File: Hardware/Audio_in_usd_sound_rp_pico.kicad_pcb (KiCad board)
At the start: 2 copper layers, 100 x 100 mm, 275 parts, among them J1 ADC IN, J11 SDR ANT, J12 SDR Out, J13 ANT_BNC, J14 ANT_BNC, J15 Audio IN, J16 Audio IN, J17 Mini-jack socket, J4 Conn_02x20_Counter_Clockwise, J5 Conn_01x20, J6 Conn_01x20, J7 Conn_02x20_Counter_Clockwise, J8 BNC, Q1 MMBT2222A 1P, Q2 MMBT2222A 1P, Q3 MMBT2222A, SW1 Left, SW2 Right, T1 Screw Terminal, 4Px5.08mm, 20A, T2 Screw Terminal, 4Px5.08mm, 20A, U1 LSM6DSO32TR, U10 Si4732, U11 HS96L03W2C03, U12 L298N, U13 LM393DR2G, U15 DS18B20A10T6, U17 LM2937xS, U2 PCM1808PWR, U3 Pico, U4 MS5351M, U5 CJ431, U6 TSOP4438, U7 PI5C3253CQEX, U8 OPA1612AxD, U9 LM358, X1 Q13FC1350000400, Y1 X322525MSB4SI

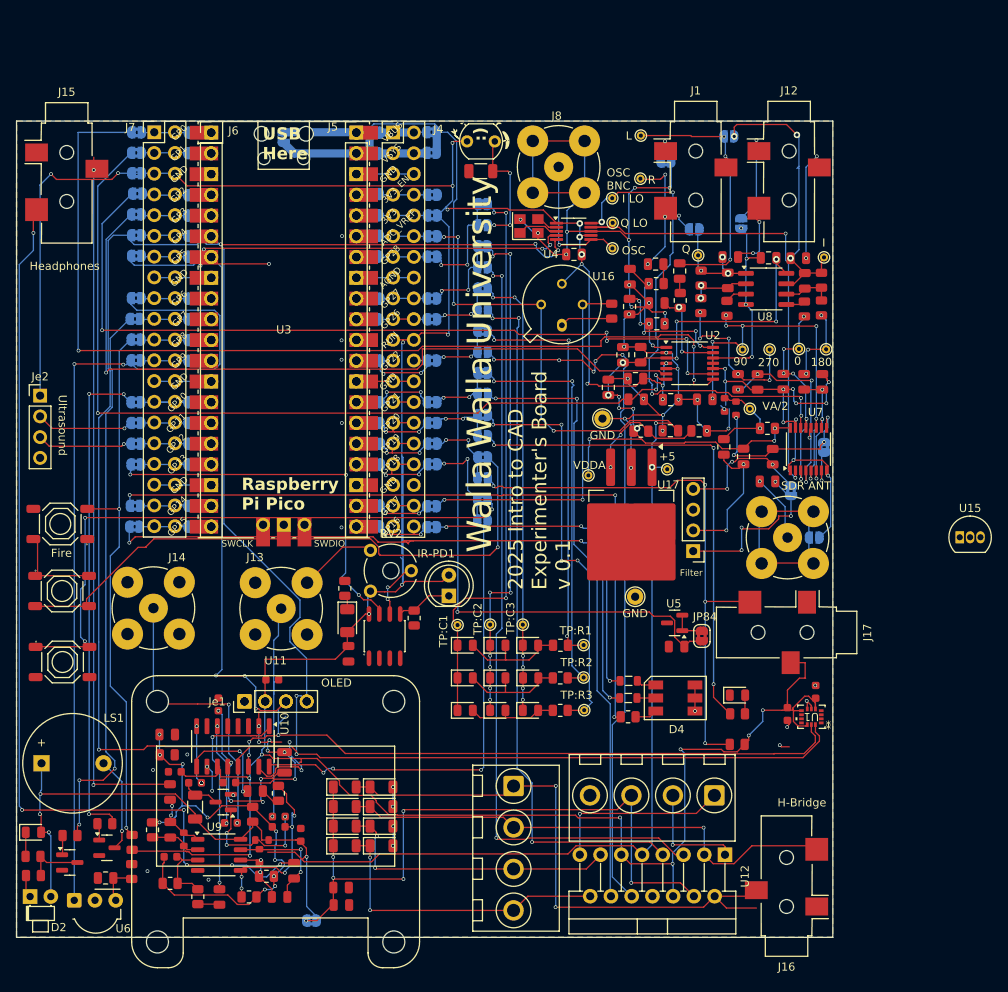
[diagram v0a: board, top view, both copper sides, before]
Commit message: Fix Si4732
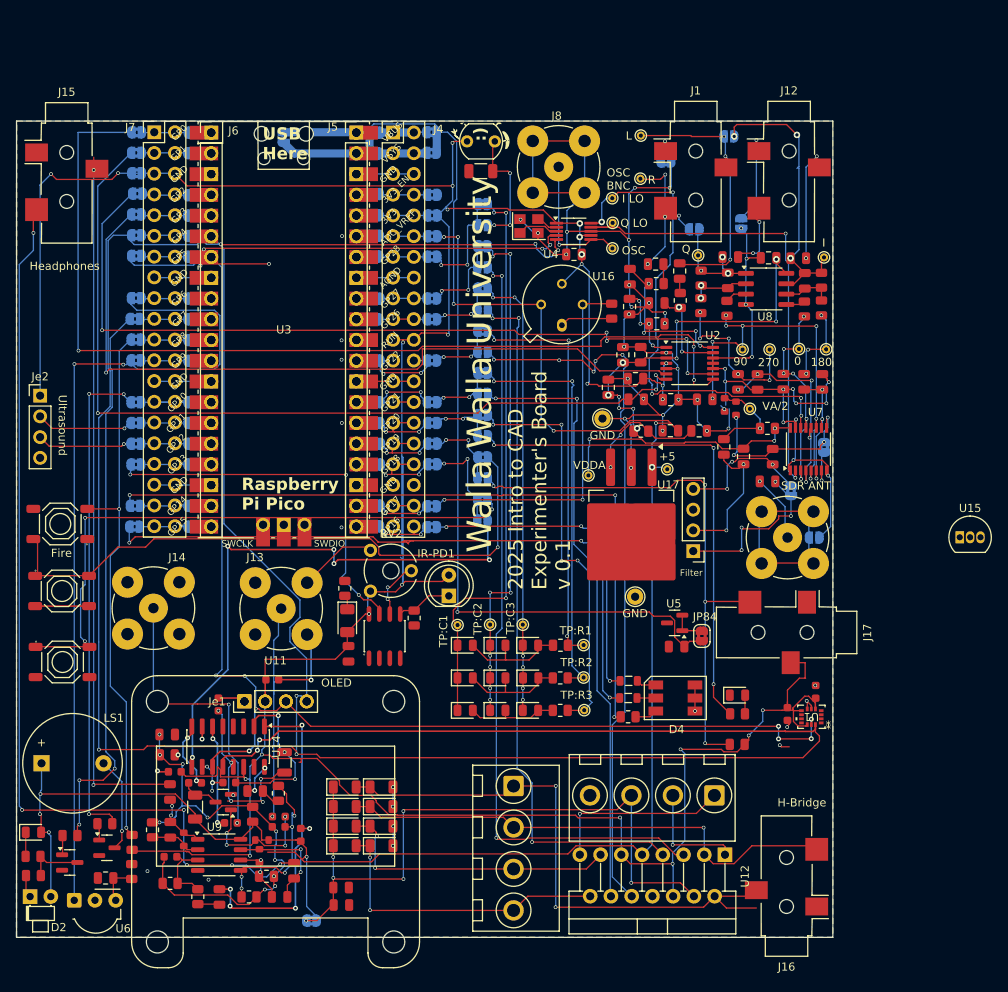
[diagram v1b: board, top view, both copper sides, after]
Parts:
- removed U10: Si4732, Package_SO:SOIC-16_3.9x9.9mm_P1.27mm
- added U14: Si4732, Package_SO:SOIC-16_3.9x9.9mm_P1.27mm, F.Cu at (113.7, 124.2)
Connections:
- net <NO NET> renamed ~
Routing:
- net /SDA: track 292.2 -> 365.4 mm, vias 6 -> 8
- net Net-(U14-LOUT): track 26.7 -> 39.0 mm, vias 2 -> 4
- net /~{RST}: track 57.6 -> 67.9 mm, vias 3 -> 5
- net GND: track 334.1 -> 342.7 mm, vias 67 -> 69
- net /RightButton: track 73.7 -> 65.2 mm
- net Net-(U14-ROUT): track 12.3 -> 4.37 mm
- net (no net): track 0.00 -> 6.60 mm
- net +3.3V: track 415.0 -> 417.1 mm
- net Net-(U14-DCLK): track 21.4 -> 20.0 mm, vias 6 -> 3
- net Net-(U14-AMI): track 7.83 -> 8.95 mm, vias 4 -> 2
- net /SCL: track 214.3 -> 213.4 mm, vias 11 -> 13
- net Net-(U14-RCLK): track 23.2 -> 22.6 mm
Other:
- copper layers 2 -> 4
